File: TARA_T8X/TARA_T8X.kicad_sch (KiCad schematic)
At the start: 0 parts

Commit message: เพื่มวงจรมาจากเดิม
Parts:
- added BT?: 3V, Battery:BatteryHolder_LINX_BAT-HLD-012-SMT, symbol Device:Battery_Cell
- added C? (x2), CR?: 100nF, Capacitor_SMD:C_0805_2012Metric, symbol Device:C_Polarized_Small_US
- added C?: 100uf/16V, Capacitor_SMD:C_0805_2012Metric, symbol Device:C_Polarized_Small_US
- added C?: 10uf/50v, Capacitor_SMD:C_0805_2012Metric, symbol Device:C_Polarized_Small_US
- added C?: 220uf/35V, Capacitor_THT:CP_Radial_D8.0mm_P5.00mm, symbol Device:C_Polarized_Small_US
- added D? (x8): 1N4007, Diode_SMD:D_1206_3216Metric, symbol Device:D_Small
- added D? (x2): 1N4148, Diode_SMD:D_1206_3216Metric, symbol Device:D_Small
- added Dled? (x2), LED? (x14): LED, LED_SMD:LED_0805_2012Metric, symbol Device:LED
- added J5B?: Conn_01x06, Connector_PinHeader_2.54mm:PinHeader_1x06_P2.54mm_Vertical, symbol Connector_Generic:Conn_01x06
- added J? (x2): Screw_Terminal_01x10, my_footprint:2EDGR-5.08-10P, symbol Connector:Screw_Terminal_01x10
- added J?: Conn_01x04_MountingPin, Connector_PinHeader_2.54mm:PinHeader_1x04_P2.54mm_Vertical, symbol Connector_Generic_MountingPin:Conn_01x04_MountingPin
- added J?: ESP32-WROOM-32U, RF_Module:ESP32-WROOM-32U, symbol RF_Module:ESP32-WROOM-32U
- added OPTO? (x14): PC817, my_footprint:SO-4_7.6x3.6mm_P2.54mm_1234, symbol Isolator:PC817
- added Q9A?, Q? (x9): 2N5401, Package_TO_SOT_SMD:SOT-23, symbol Device:Q_PNP_BCE
- added R? (x30), RL? (x4), R_led? (x2), Ren?: 560, Resistor_SMD:R_0805_2012Metric, symbol Device:R_Small
- added R? (x8), Rbo?: 10K, Resistor_SMD:R_0805_2012Metric, symbol Device:R_Small
- added RF? (x2): 0, Resistor_SMD:R_0805_2012Metric, symbol Device:R_Small
- added RT? (x2): 3.3K, Resistor_SMD:R_0805_2012Metric, symbol Device:R_Small
- added S? (x4): SW_Push, Button_Switch_THT:SW_PUSH_6mm_H5mm, symbol Switch:SW_Push
- added U?: DS1307+, Package_SO:SOIC-8-1EP_3.9x4.9mm_P1.27mm_EP2.29x3mm, symbol Timer_RTC:DS1307+
- added U?: LM1117-3.3, Package_TO_SOT_SMD:SOT-223-3_TabPin2, symbol Regulator_Linear:LM1117-3.3
- added U?: TTL_RS485_Module, my_footprint:RS485-TTL, symbol 1_MyDevice:TTL_RS485_Module
- added U?: CN3903, my_footprint:DCDC5V, symbol 1_MyDevice:CN3903
- added Y?: Crystal_Small, Crystal:Crystal_AT310_D3.0mm_L10.0mm_Horizontal, symbol Device:Crystal_Small
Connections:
- new net: LED?.2 (A), RL?.1
- new net: J?.1 (Pin_1), R?.2, RL?.2
- new net: D?.1 (K), J?.7 (Pin_7), LED?.2 (A), Q?.3 (C)
- new net: Q?.1 (B), R?.1 (x9)
- new net: OPTO?.4, R?.2 (x10)
- new net: J?.2 (Pin_2), R?.2, RL?.1
- new net: J?.3 (Pin_3), R?.1, RL?.1
- new net: J?.4 (Pin_4), R?.1, RL?.1
- new net: J?.5 (Pin_5), LED?.1 (K), LED?.1 (K), LED?.1 (K), LED?.1 (K), OPTO?.2, OPTO?.2, OPTO?.2, OPTO?.2
- new net: LED?.1 (K), R?.1 (x9)
- new net: OPTO?.1, R?.1 (x10)
- new net: J?.23 (IO15), R?.2
- new net: Q9A?.1 (B), R?.1
- new net: OPTO?.1, R?.2 (x4)
- new net: J?.2 (Pin_3), J?.33 (IO21), RF?.2, RT?.1, U?.5 (SDA)
- new net: D?.1 (K), J?.5 (Pin_5), LED?.2 (A), Q?.3 (C)
- new net: Dled?.2 (A), R_led?.2 (x2)
- new net: D?.1 (K), J?.4 (Pin_4), LED?.2 (A), Q?.3 (C)
- new net: D?.1 (K), J?.2 (Pin_2), LED?.2 (A), Q?.3 (C)
- new net: J?.1 (Pin_2), J?.36 (IO22), RF?.2, RT?.1, U?.6 (SCL)
- new net: D?.1 (K), J?.6 (Pin_6), LED?.2 (A), Q?.3 (C)
- new net: J?.6 (IO34), R?.1, S?.1
- new net: J?.29 (IO5), OPTO?.4
- new net: LED?.2 (A), RL?.2 (x3)
- new net: D?.1 (K), J?.3 (Pin_3), LED?.2 (A), Q?.3 (C)
- new net: J?.13 (IO14), R?.1
- new net: J?.7 (IO35), R?.1, S?.1
- new net: J?.4 (SENSOR_VP), R?.1, S?.1
- new net: J?.30 (IO18), OPTO?.4
- new net: D?.1 (K), J?.8 (Pin_8), LED?.2 (A), Q?.3 (C)
- new net: J?.31 (IO19), OPTO?.4
- new net: J?.14 (IO12), R?.2
- new net: J?.9 (IO33), R?.2
- new net: D?.1 (K), J?.9 (Pin_9), LED?.2 (A), Q?.3 (C)
- new net: U?.1 (X1), Y?.1
- new net: U?.2 (X2), Y?.2
- new net: BT?.1 (+), U?.3 (VBAT)
- new net: D?.1 (K), J?.1 (Pin_1), LED?.2 (A), Q?.3 (C)
- new net: D?.1 (K), J?.10 (Pin_10), LED?.2 (A), Q9A?.3 (C)
- new net: J?.37 (IO23), OPTO?.4
- new net: J?.16 (IO13), R?.2
- new net: J?.10 (IO25), R?.1
- new net: J?.11 (IO26), R?.2
- new net: J?.12 (IO27), R?.2
- new net: J?.24 (IO2), R_led?.1
- new net: J?.26 (IO4), R?.2
- new net: J5B?.2 (Pin_2), J?.34 (RXD0/IO3)
- new net: J5B?.1 (Pin_1), J?.35 (TXD0/IO1)
- new net: J?.5 (SENSOR_VN), R?.1, S?.1
- new net: J?.8 (IO32), R?.2
- new net: LED?.1 (K), R?.2
- new net 3V3: C?.1, C?.1, J5B?.3 (Pin_3), J?.2 (VDD), RT?.2, RT?.2, R_led?.1, Rbo?.1, Ren?.1, S?.2, S?.2, S?.2, S?.2, U?.1 (VCC), U?.2 (VO)
- new net 5V: C?.1, C?.1, J?.3 (Pin_1), U?.3 (VI), U?.4 (VOUT+), U?.8 (VCC)
- new net A: J?.7 (Pin_7), RF?.1, U?.7 (A)
- new net B: J?.6 (Pin_6), RF?.1, U?.6 (B)
- new net BOOT: J5B?.6 (Pin_6), J?.25 (IO0), Ren?.2
- new net EN: CR?.1, J5B?.5 (Pin_5), J?.3 (EN), Rbo?.2
- new net GND: BT?.2 (-), C?.2, C?.2, C?.2, C?.2, C?.2, CR?.2, D?.2 (A), D?.2 (A), D?.2 (A), D?.2 (A), D?.2 (A), D?.2 (A), D?.2 (A), D?.2 (A), D?.2 (A), D?.2 (A), Dled?.1 (K), Dled?.1 (K), J5B?.4 (Pin_4), J?.1 (GND), J?.15 (GND), J?.38 (GND), J?.39 (GND), J?.4 (Pin_4), J?.8 (Pin_8), OPTO?.2, OPTO?.2, OPTO?.2, OPTO?.2, OPTO?.2, OPTO?.2, OPTO?.2, OPTO?.2, OPTO?.2, OPTO?.2, OPTO?.3, OPTO?.3, OPTO?.3, OPTO?.3, OPTO?.3, OPTO?.3, OPTO?.3, OPTO?.3, OPTO?.3, OPTO?.3, OPTO?.3, OPTO?.3, OPTO?.3, OPTO?.3, R?.1, R?.2, R?.2, R?.2, R?.2, R?.2, R?.2, R?.2, R?.2, R?.2, R?.2, R?.2, R?.2, R?.2, U?.1 (GND), U?.2 (VIN-), U?.3 (VOUT-), U?.4 (GND), U?.4 (GND), U?.5 (GND)
- new net GPIO16: J?.27 (IO16), U?.2 (TXD)
- new net GPIO17: J?.28 (IO17), U?.3 (RXD)
- new net VCC: J?.10 (Pin_10), Q9A?.2 (E), Q?.2 (E), Q?.2 (E), Q?.2 (E), Q?.2 (E), Q?.2 (E), Q?.2 (E), Q?.2 (E), Q?.2 (E), Q?.2 (E)
- new net VCC2: C?.1, J?.9 (Pin_9), U?.1 (VIN+)
- no-connect marks 0 -> 8
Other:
- note added: "LCD"

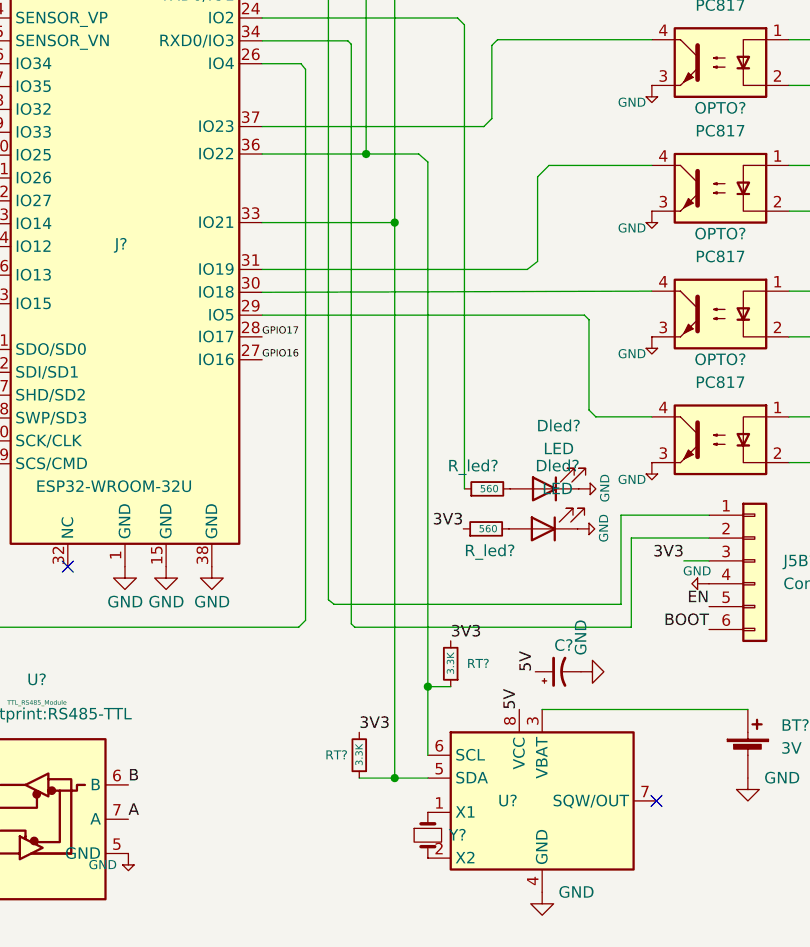
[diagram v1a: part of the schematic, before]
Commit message: ยกเลิก R-Pullup 47K
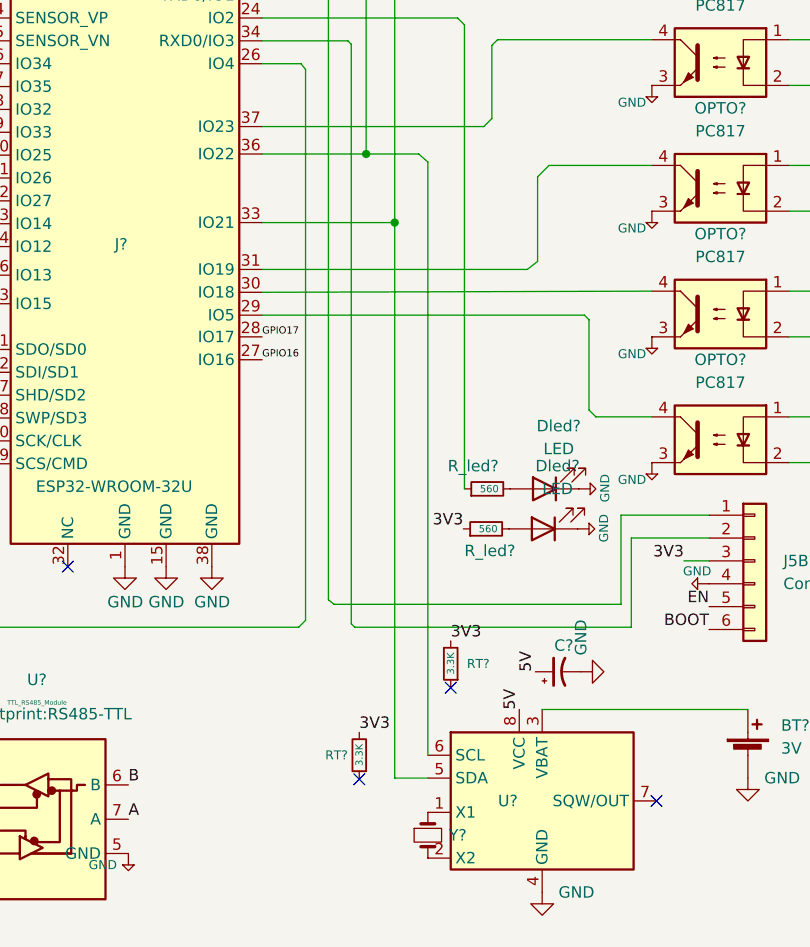
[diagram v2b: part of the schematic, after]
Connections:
- net at J?.2 (Pin_3), J?.33 (IO21), RF?.2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: no longer RT?.1
- net at J?.1 (Pin_2), J?.36 (IO22), RF?.2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: no longer RT?.1
- no-connect marks 8 -> 10
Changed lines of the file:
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@@
   (junction (at 123.698 156.083) (diameter 0) (color 0 0 0 0)
   )
-  (junction (at 260.477 187.325) (diameter 0) (color 0 0 0 0)
-  )
   (junction (at 319.532 84.328) (diameter 0) (color 0 0 0 0)
   )
@@
   )
   (junction (at 314.452 90.678) (diameter 0) (color 0 0 0 0)
-  )
-  (junction (at 264.16 177.165) (diameter 0) (color 0 0 0 0)
   )
   (junction (at 195.707 107.95) (diameter 0) (color 0 0 0 0)
@@
   (no_connect (at 215.265 149.86))
   (no_connect (at 215.265 147.32))
+  (no_connect (at 266.7 177.292))
   (no_connect (at 215.265 152.4))
   (no_connect (at 224.155 163.83))
   (no_connect (at 215.265 139.7))
   (no_connect (at 215.265 144.78))
+  (no_connect (at 256.54 187.452))
   (no_connect (at 215.265 142.24))
   (wire (pts (xy 95.123 117.348) (xy 95.123 216.408))
@@
     (stroke (width 0) (type default) (color 0 0 0 0))
   )
-  (wire (pts (xy 264.16 118.872) (xy 264.16 177.165))
-    (stroke (width 0) (type default) (color 0 0 0 0))
-  )
   (wire (pts (xy 143.383 227.203) (xy 138.303 227.203))
     (stroke (width 0) (type default) (color 0 0 0 0))
@@
     (stroke (width 0) (type default) (color 0 0 0 0))
   )
-  (wire (pts (xy 264.16 177.165) (xy 266.7 177.165))
-    (stroke (width 0) (type default) (color 0 0 0 0))
-  )
   (wire (pts (xy 304.292 133.223) (xy 316.992 133.223))
     (stroke (width 0) (type default) (color 0 0 0 0))
@@
     (stroke (width 0) (type default) (color 0 0 0 0))
   )
-  (wire (pts (xy 256.54 187.325) (xy 260.477 187.325))
-    (stroke (width 0) (type default) (color 0 0 0 0))
-  )
   (wire (pts (xy 113.538 96.393) (xy 114.173 95.758))
     (stroke (width 0) (type default) (color 0 0 0 0))
@@
     (stroke (width 0) (type default) (color 0 0 0 0))
   )
-  (wire (pts (xy 264.16 177.165) (xy 264.16 184.785))
-    (stroke (width 0) (type default) (color 0 0 0 0))
-  )
+  (wire (pts (xy 264.16 118.872) (xy 264.16 184.785))
+    (stroke (width 0) (type default) (color 0 0 0 0))
+  )

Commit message: PCB-V2.8.3
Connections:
- net at RT?.1: now also J?.2 (Pin_3), J?.33 (IO21), RF?.2, U?.5 (SDA)
- net at J?.1 (Pin_2), J?.36 (IO22), RF?.2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: now also RT?.1
- no-connect marks 10 -> 8
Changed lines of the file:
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@@
   (junction (at 116.713 124.333) (diameter 0) (color 0 0 0 0)
   )
+  (junction (at 264.16 177.165) (diameter 0) (color 0 0 0 0)
+  )
   (junction (at 116.713 140.843) (diameter 0) (color 0 0 0 0)
   )
@@
   )
   (junction (at 257.302 87.376) (diameter 0) (color 0 0 0 0)
+  )
+  (junction (at 260.477 187.325) (diameter 0) (color 0 0 0 0)
   )
   (junction (at 212.217 89.789) (diameter 0) (color 0 0 0 0)
@@
   (no_connect (at 215.265 149.86))
   (no_connect (at 215.265 147.32))
-  (no_connect (at 266.7 177.292))
   (no_connect (at 215.265 152.4))
   (no_connect (at 224.155 163.83))
   (no_connect (at 215.265 139.7))
   (no_connect (at 215.265 144.78))
-  (no_connect (at 256.54 187.452))
   (no_connect (at 215.265 142.24))
   (wire (pts (xy 95.123 117.348) (xy 95.123 216.408))
@@
     (stroke (width 0) (type default) (color 0 0 0 0))
   )
+  (wire (pts (xy 256.54 187.325) (xy 260.477 187.325))
+    (stroke (width 0) (type default) (color 0 0 0 0))
+  )
   (wire (pts (xy 191.516 102.87) (xy 200.787 102.87))
     (stroke (width 0) (type default) (color 0 0 0 0))
@@
     (stroke (width 0) (type default) (color 0 0 0 0))
   )
+  (wire (pts (xy 264.16 177.165) (xy 264.16 184.785))
+    (stroke (width 0) (type default) (color 0 0 0 0))
+  )
   (wire (pts (xy 189.103 172.085) (xy 190.754 170.561))
     (stroke (width 0) (type default) (color 0 0 0 0))
@@
     (stroke (width 0) (type default) (color 0 0 0 0))
   )
+  (wire (pts (xy 266.7 177.165) (xy 264.16 177.165))
+    (stroke (width 0) (type default) (color 0 0 0 0))
+  )
   (wire (pts (xy 116.713 156.083) (xy 123.698 156.083))
     (stroke (width 0) (type default) (color 0 0 0 0))
@@
     (stroke (width 0) (type default) (color 0 0 0 0))
   )
-  (wire (pts (xy 264.16 118.872) (xy 264.16 184.785))
-    (stroke (width 0) (type default) (color 0 0 0 0))
-  )
+  (wire (pts (xy 264.16 118.872) (xy 264.16 177.165))
+    (stroke (width 0) (type default) (color 0 0 0 0))
+  )

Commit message: gerber PCB-V2.8.3
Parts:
- gave numbers to parts that had none: 121

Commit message: ล่าสุดวันเสาร์ที่4ตุลาคม68
rer
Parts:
- removed J5B1: Conn_01x06, Connector_PinHeader_2.54mm:PinHeader_1x06_P2.54mm_Vertical, symbol Connector_Generic:Conn_01x06
- J2: footprint RF_Module:ESP32-WROOM-32U -> RF_Module:ESP32-S3-WROOM-1
- RF2: value 0 -> 0
- renumbered Q9A1 to Q10
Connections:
- net IO04: now reaches J2.26 (IO4), R30.2
- no-connect marks 8 -> 10
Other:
- moved on the sheet: BT1, C1, C2, C3, C4, C5, CR1, D1, D10, D2, D3, D4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

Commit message: 202510041905
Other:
- note added: "TARA_T8X"
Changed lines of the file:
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@@
 	(generator_version "9.0")
 	(paper "A3")
+	(text "TARA_T8X"
+		(exclude_from_sim no)
+		(at 219.456 236.728 0)
+		(effects
+			(font
+				(size 5 5)
+			)
+		)
+	)
 	(text "LCD"
 		(exclude_from_sim no)

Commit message: 202506100619_home_win10_kicad9
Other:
- moved on the sheet: BT1, C1, C2, C3, C4, C5, CR1, D1, D10, D2, D3, D4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

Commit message: 202510071819_greensave
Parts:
- J1, J4: footprint my_footprint:2EDGR-5.08-10P -> TerminalBlock:TerminalBlock_MaiXu_MX126-5.0-10P_1x10_P5.00mm
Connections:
- net VCC2 is gone; now on net VCC: C1.1, J4.9 (Pin_9), U1.1 (VIN+)
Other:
- moved on the sheet: BT1, C1, C2, C3, C4, C5, CR1, D1, D10, D2, D3, D4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
